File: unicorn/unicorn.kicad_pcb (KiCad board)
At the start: 2 copper layers, 35 x 75 mm, 26 parts, among them J0 Conn_01x02, J1 Conn_01x14_Female, J2 Conn_01x14_Female, J3 Conn_02x03_Odd_Even, U1 ATmega328-P, U2 L7805

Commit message: add fp anch sym table settings and fix the projects
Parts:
- J3: value Conn_02x03_Odd_Even -> SPI
- LED1: value Pwr -> PWR
- LED2: value Rst -> RST
- RST1: value Reset -> TACT Reset
- U2: footprint Transistor_Power_Module:TO255P1020X450X2000-3 -> L7805:TO255P1020X450X2000-3
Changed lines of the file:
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@@
         (effects (font (size 1 1) (thickness 0.15)))
     )
-    (fp_text value "Pwr" (at -2.12 0.0475 180) (layer "F.SilkS")
+    (fp_text value "PWR" (at -2.12 0.0475 180) (layer "F.SilkS")
         (effects (font (size 1 1) (thickness 0.15)))
     )
@@
         (effects (font (size 1 1) (thickness 0.15)))
     )
-    (fp_text value "Rst" (at -2.12 -0.0525 180) (layer "F.SilkS")
+    (fp_text value "RST" (at -2.12 -0.0525 180) (layer "F.SilkS")
         (effects (font (size 1 1) (thickness 0.15)))
     )
@@
     )
   )
-  (footprint "Transistor_Power_Module:TO255P1020X450X2000-3" (layer "F.Cu")
+  (footprint "L7805:TO255P1020X450X2000-3" (layer "F.Cu")
     (at 129.877 77 -90)
     (property "Sheetfile" "unicorn.kicad_sch")
@@
         (effects (font (size 1 1) (thickness 0.15)))
     )
-    (fp_text value "Reset" (at 3.37 -2.6 270) (layer "F.SilkS")
+    (fp_text value "TACT Reset" (at 3.37 -2.6 270) (layer "F.SilkS")
         (effects (font (size 1 1) (thickness 0.15)))
     )
@@
         (effects (font (size 1 1) (thickness 0.15)))
     )
-    (fp_text value "Conn_02x03_Odd_Even" (at 1.27 7.68) (layer "F.SilkS") hide
-        (effects (font (size 1 1) (thickness 0.15)))
-    )
+    (fp_text value "SPI" (at 1.27 7.68) (layer "F.SilkS") hide
+        (effects (font (size 1 1) (thickness 0.15)))
+    )

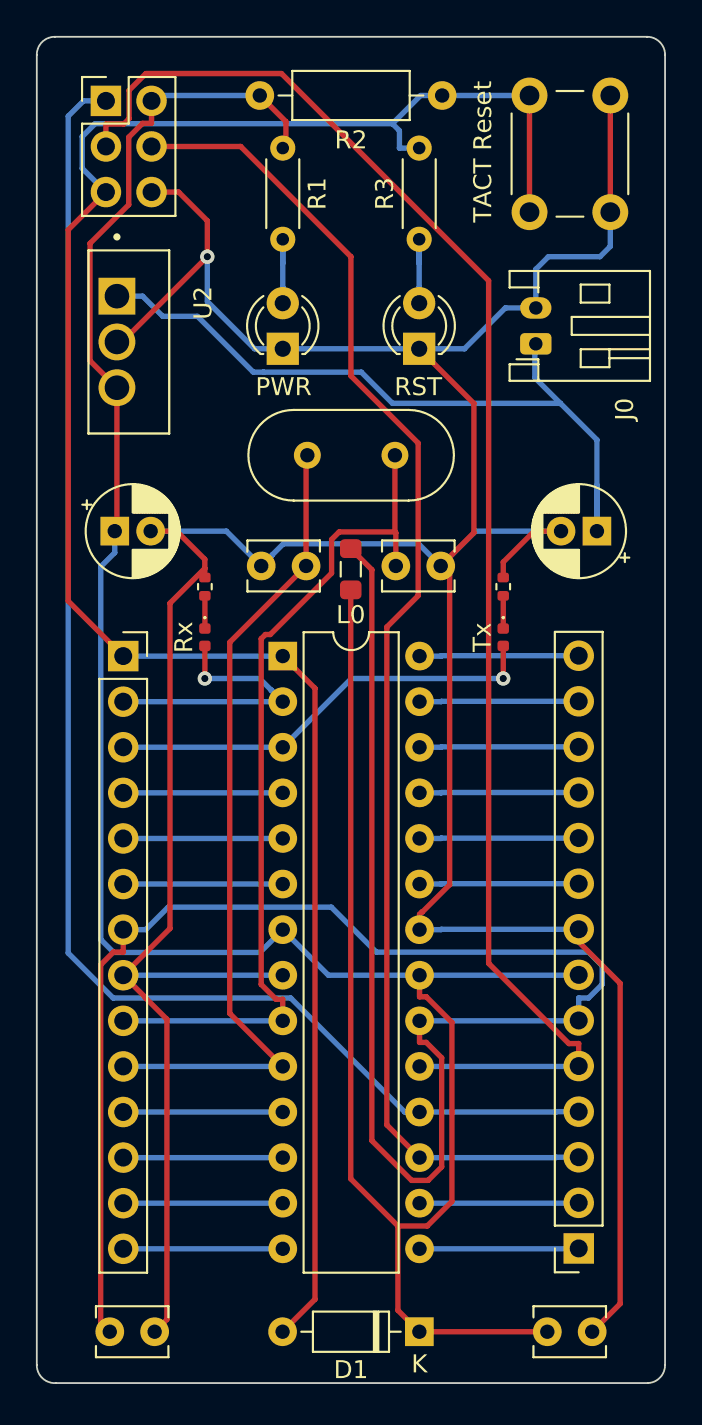
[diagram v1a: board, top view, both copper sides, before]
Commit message: replace power connector - still need to redo routing
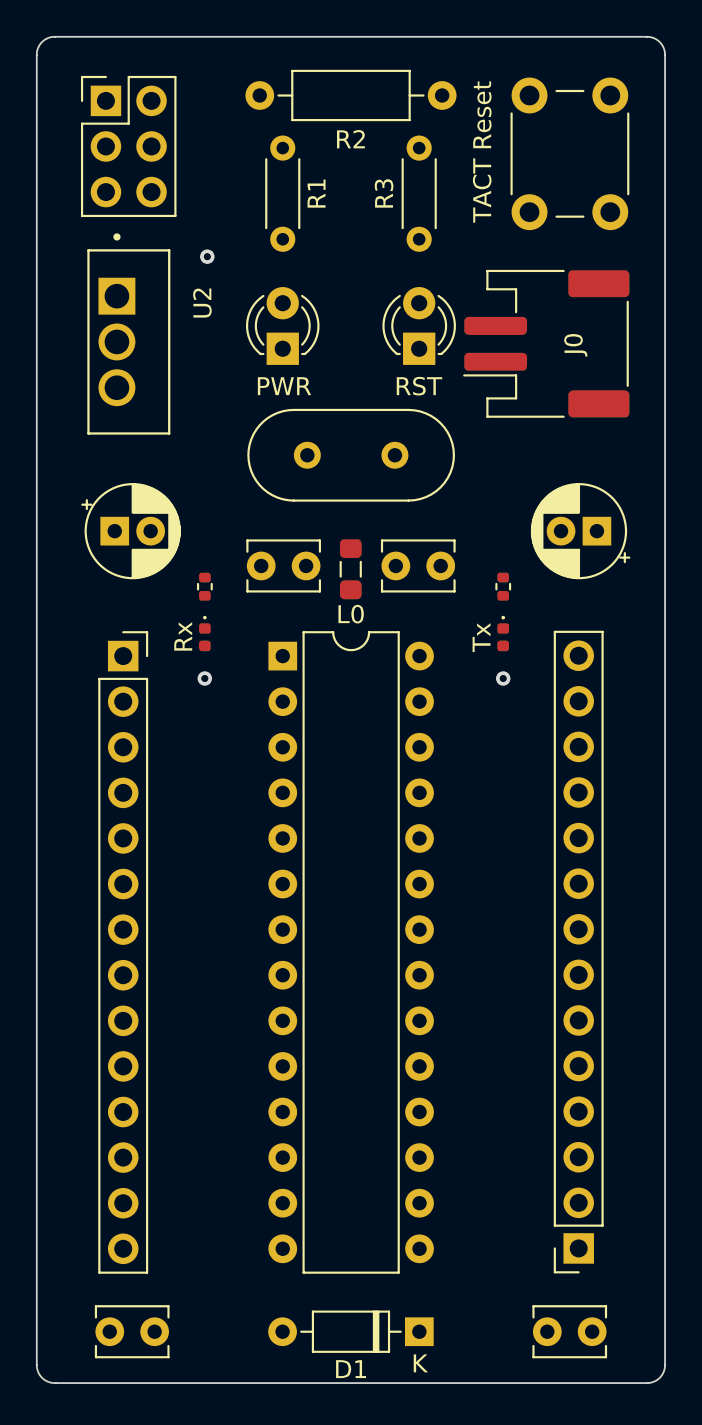
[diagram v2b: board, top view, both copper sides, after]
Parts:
- J0: footprint Connector_JST:JST_PH_S2B-PH-K_1x02_P2.00mm_Horizontal -> Connector_JST:JST_PH_S2B-PH-SM4-TB_1x02-1MP_P2.00mm_Horizontal
- moved J0 0.61 mm to (153.2, 77.1)
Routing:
- net GND: track 209.5 -> 0.00 mm
- net Net-(D1-K): track 155.0 -> 0.00 mm
- net Net-(D1-A): track 114.6 -> 0.00 mm
- net Net-(J1-Pin_6): track 112.2 -> 0.00 mm
- net Net-(J1-Pin_5): track 84.5 -> 0.00 mm
- net Net-(J1-Pin_4): track 81.2 -> 0.00 mm
- net Net-(J1-Pin_3): track 75.7 -> 0.00 mm
- net Net-(J2-Pin_9): track 48.1 -> 0.00 mm
- net Net-(J2-Pin_10): track 46.0 -> 0.00 mm
- net Net-(J0-Pin_1): track 41.6 -> 0.00 mm
- net Net-(J2-Pin_3): track 24.6 -> 0.00 mm
- net Net-(J2-Pin_2): track 16.5 -> 0.00 mm
- net Net-(J2-Pin_6): track 8.89 -> 0.00 mm
- net Net-(J2-Pin_5): track 8.89 -> 0.00 mm
- net Net-(J2-Pin_4): track 8.89 -> 0.00 mm
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
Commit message: fix routing + replace power connector with the right one
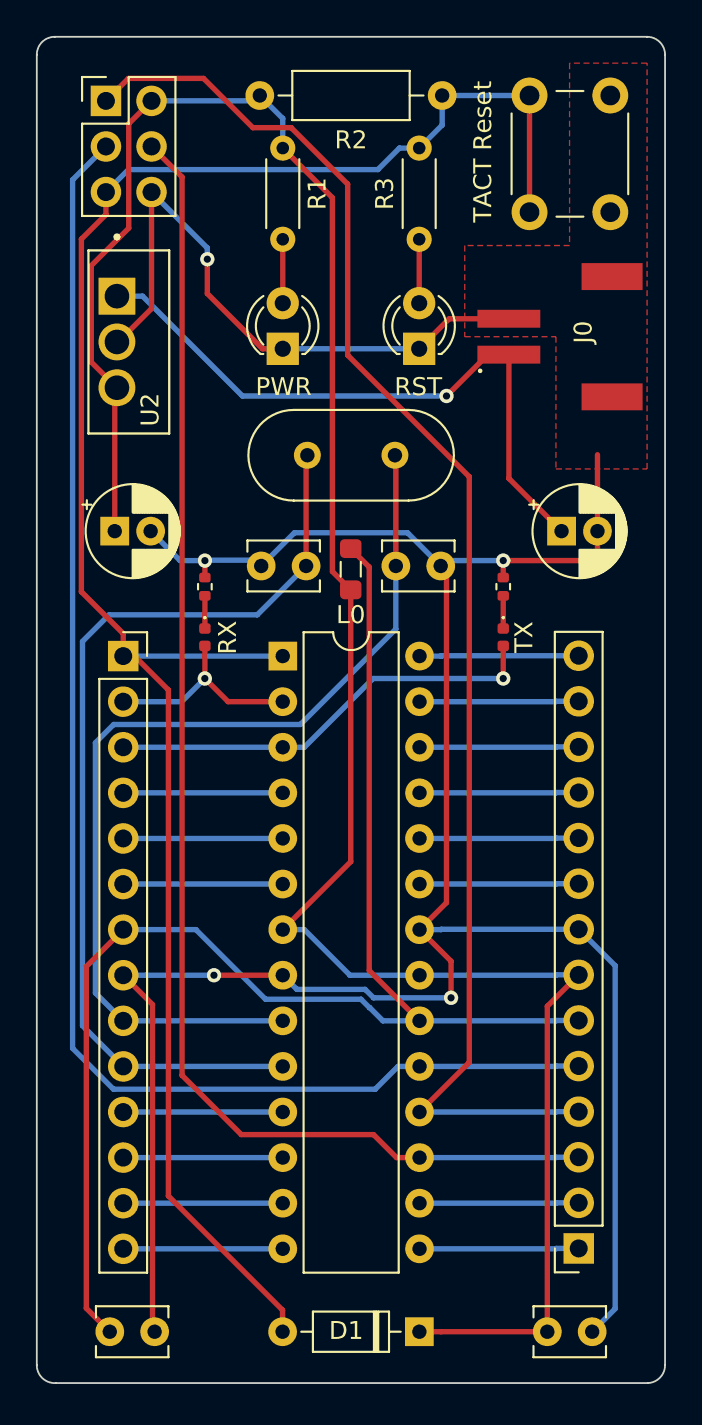
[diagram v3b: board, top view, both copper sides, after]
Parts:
- J0: footprint Connector_JST:JST_PH_S2B-PH-SM4-TB_1x02-1MP_P2.00mm_Horizontal -> JST_S2B-PH-SM4-TB:JST_S2B-PH-SM4-TB
- LED3: value Tx -> TX
- LED4: value Rx -> RX
- moved J0 2.15 mm to (151.0, 76.7), turned to -90 degrees
- moved C1 1.97 mm to (154.0, 87.5), turned to 0 degrees
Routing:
- net GND: track 0.00 -> 167.3 mm, vias 1 -> 5
- net Net-(D1-K): track 0.00 -> 127.6 mm
- net Net-(D1-A): track 0.00 -> 111.2 mm
- net Net-(J1-Pin_4): track 0.00 -> 80.9 mm
- net Net-(J1-Pin_5): track 0.00 -> 80.7 mm
- net Net-(J1-Pin_6): track 0.00 -> 79.2 mm
- net Net-(J1-Pin_3): track 0.00 -> 76.5 mm
- net Net-(J2-Pin_9): track 0.00 -> 55.0 mm
- net Net-(J2-Pin_10): track 0.00 -> 53.9 mm
- net Net-(J0-Pin_1): track 0.00 -> 36.1 mm, vias 0 -> 1
- net Net-(J2-Pin_3): track 0.00 -> 24.6 mm
- net Net-(J2-Pin_2): track 0.00 -> 11.8 mm
- net Net-(J2-Pin_6): track 0.00 -> 8.89 mm
- net Net-(J2-Pin_5): track 0.00 -> 8.89 mm
- net Net-(J2-Pin_4): track 0.00 -> 8.89 mm
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- added copper zone on F.Cu, net GND
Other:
- board text added: "Unicorn rev_B"
- board text removed: "First sgiraz pcb"

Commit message: update unicorn board layout - minor improvements to the project footprints
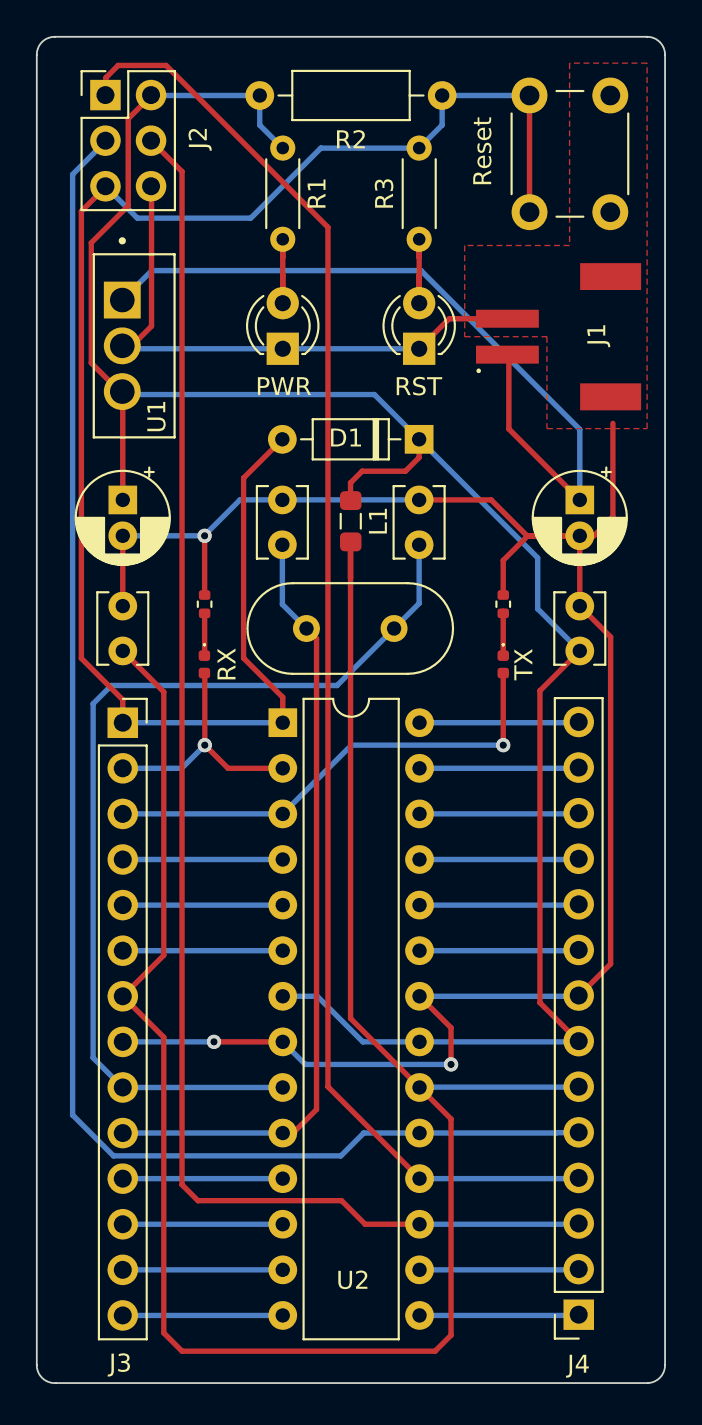
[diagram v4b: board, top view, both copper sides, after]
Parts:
- removed J0: Conn_01x02, JST_S2B-PH-SM4-TB:JST_S2B-PH-SM4-TB
- removed L0: 10uH, Inductor_SMD:L_0805_2012Metric_Pad1.05x1.20mm_HandSolder
- added J4: Conn_01x14_Female, Connector_PinSocket_2.54mm:PinSocket_1x14_P2.54mm_Vertical, F.Cu at (154.9, 131.2)
- added L1: 10uH, Inductor_SMD:L_0805_2012Metric_Pad1.05x1.20mm_HandSolder, F.Cu at (142.2, 87.0)
- J1: value Conn_01x14_Female -> Conn_01x02; footprint Connector_PinSocket_2.54mm:PinSocket_1x14_P2.54mm_Vertical -> JST_S2B-PH-SM4-TB:JST_S2B-PH-SM4-TB
- J2: value Conn_01x14_Female -> SPI; footprint Connector_PinSocket_2.54mm:PinSocket_1x14_P2.54mm_Vertical -> Connector_PinHeader_2.54mm:PinHeader_2x03_P2.54mm_Vertical
- J3: value SPI -> Conn_01x14_Female; footprint Connector_PinHeader_2.54mm:PinHeader_2x03_P2.54mm_Vertical -> Connector_PinSocket_2.54mm:PinSocket_1x14_P2.54mm_Vertical
- RST1: value TACT Reset -> Reset
- U1: value ATmega328-P -> L7805; footprint Package_DIP:DIP-28_W7.62mm -> L7805:TO255P1020X450X2000-3
- U2: value L7805 -> ATmega328-P; footprint L7805:TO255P1020X450X2000-3 -> Package_DIP:DIP-28_W7.62mm
- moved J1 50.9 mm to (151.0, 76.7), turned to -90 degrees
- moved D1 49.7 mm to (146.1, 82.4)
- moved C6 40.5 mm to (129.5, 91.7), turned to -90 degrees
- moved C3 38.0 mm to (155.0, 94.2), turned to 90 degrees
- moved J3 34.7 mm to (129.5, 98.2)
- moved J2 31.3 mm to (128.6, 63.2)
- moved U2 22.9 mm to (138.5, 98.2), turned to 0 degrees
- moved U1 19.2 mm to (130.2, 77.2), turned to -90 degrees
- moved Crystal1 9.65 mm to (144.7, 93.0)
- moved C5 3.86 mm to (138.4, 85.8), turned to -90 degrees
- moved C1 2.01 mm to (155.0, 85.8), turned to -90 degrees
- moved C2 1.80 mm to (129.5, 85.8), turned to -90 degrees
- moved C4 1.75 mm to (146.1, 88.3), turned to 90 degrees
- moved LED4 1.51 mm to (134.1, 95.0)
- moved LED3 1.51 mm to (150.7, 95.0)
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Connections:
- C1 pad 1: Net-(J0-Pin_1) -> Net-(J1-Pin_1)
- C4 pad 1: Net-(J2-Pin_9) -> Net-(J3-Pin_9)
- C5 pad 2: Net-(J2-Pin_10) -> Net-(J3-Pin_10)
- C6 pad 2: Net-(J1-Pin_6) -> Net-(J3-Pin_7)
- Crystal1 pad 1: Net-(J2-Pin_9) -> Net-(J3-Pin_9)
- Crystal1 pad 2: Net-(J2-Pin_10) -> Net-(J3-Pin_10)
- J1 pad 2: Net-(J1-Pin_2) -> GND
- J2 pad 1: Net-(D1-A) -> Net-(J2-Pin_1)
- J2 pad 2: Net-(J2-Pin_2) -> Net-(D1-K)
- J2 pad 5: Net-(J2-Pin_5) -> Net-(D1-A)
- J2 pad 6: Net-(J2-Pin_6) -> GND
- J3 pad 1: Net-(J1-Pin_4) -> Net-(D1-A)
- J3 pad 2: Net-(D1-K) -> Net-(J3-Pin_2)
- J3 pad 3: Net-(J1-Pin_5) -> Net-(J3-Pin_3)
- J3 pad 4: Net-(J1-Pin_3) -> Net-(J3-Pin_4)
- J3 pad 5: Net-(D1-A) -> Net-(J3-Pin_5)
- J3 pad 6: GND -> Net-(J3-Pin_6)
- LED3 pad 2: Net-(J2-Pin_3) -> Net-(J3-Pin_3)
- LED4 pad 2: Net-(J2-Pin_2) -> Net-(J3-Pin_2)
- U1 pad 1: Net-(D1-A) -> Net-(J1-Pin_1)
- U1 pad 2: Net-(J2-Pin_2) -> GND
- U1 pad 3: Net-(J2-Pin_3) -> Net-(D1-K)
- U2 pad 1: Net-(J0-Pin_1) -> Net-(D1-A)
- U2 pad 2: GND -> Net-(J3-Pin_2)
- U2 pad 3: Net-(D1-K) -> Net-(J3-Pin_3)
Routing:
- net Net-(J3-Pin_7): track 0.00 -> 114.9 mm
- net Net-(J2-Pin_1): track 0.00 -> 81.4 mm
- net Net-(J1-Pin_4): track 80.9 -> 0.00 mm
- net Net-(J1-Pin_5): track 80.7 -> 0.00 mm
- net Net-(J1-Pin_6): track 79.2 -> 0.00 mm
- net Net-(J1-Pin_3): track 76.5 -> 0.00 mm
- net Net-(J2-Pin_4): track 8.89 -> 81.8 mm
- net Net-(J2-Pin_3): track 24.6 -> 84.7 mm, vias 1 -> 0
- net Net-(J2-Pin_9): track 55.0 -> 0.00 mm
- net Net-(J3-Pin_9): track 0.00 -> 54.7 mm
- net Net-(J2-Pin_10): track 53.9 -> 0.00 mm
- net Net-(J3-Pin_10): track 0.00 -> 43.6 mm
- net Net-(J0-Pin_1): track 36.1 -> 0.00 mm, vias 1 -> 0
- net Net-(J1-Pin_1): track 8.88 -> 43.4 mm
- net GND: track 167.3 -> 139.7 mm, vias 5 -> 3
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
